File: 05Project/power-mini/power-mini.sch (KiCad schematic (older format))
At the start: 4 parts, among them J1 Conn_01x02, J2 Conn_01x02, U1 GL2576-12TB5T

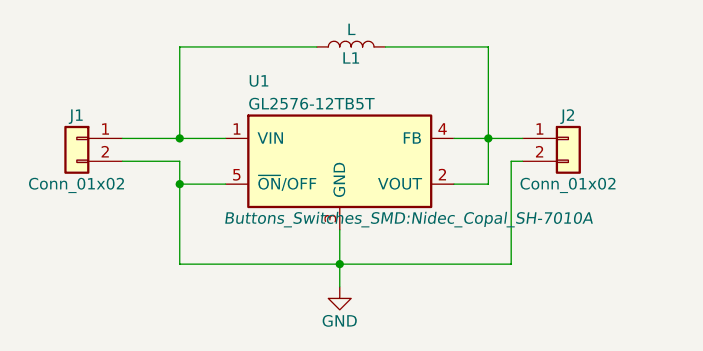
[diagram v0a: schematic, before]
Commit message: Schematic bluetooth Speaker
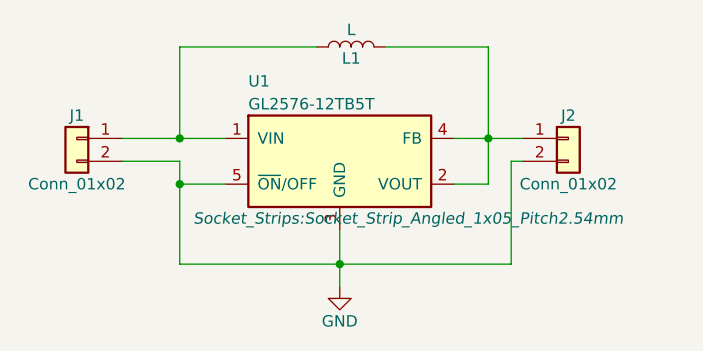
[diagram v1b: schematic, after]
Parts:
- J1: footprint Connectors:Banana_Jack_2Pin -> Connectors:PINHEAD1-2
- J2: footprint Connectors:GS2 -> Connectors:PINHEAD1-2
- L1: footprint Connectors:BNC -> Inductors_THT:L_Axial_L5.3mm_D2.2mm_P2.54mm_Vertical_Vishay_IM-1
- U1: footprint Buttons_Switches_SMD:Nidec_Copal_SH-7010A -> Socket_Strips:Socket_Strip_Angled_1x05_Pitch2.54mm
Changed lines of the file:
@@
 LIBS:valves
 LIBS:dc-dc
+LIBS:open-project
+LIBS:tom_kicad
+LIBS:w_device
+LIBS:esp32-wrover-v3
+LIBS:esp-uno
+LIBS:esp-wroom-32
+LIBS:power-mini-cache
 EELAYER 25 0
 EELAYER END
@@
 F 0 "U1" H 1900 1850 50  0000 L CNN
 F 1 "GL2576-12TB5T" H 1900 1750 50  0000 L CNN
-F 2 "Buttons_Switches_SMD:Nidec_Copal_SH-7010A" H 2600 1250 50  0000 C CIN
+F 2 "Socket_Strips:Socket_Strip_Angled_1x05_Pitch2.54mm" H 2600 1250 50  0000 C CIN
 F 3 "" H 2300 1500 50  0000 C CNN
 	1    2300 1500
@@
 F 0 "J1" H 1150 1500 50  0000 C CNN
 F 1 "Conn_01x02" H 1150 1200 50  0000 C CNN
-F 2 "Connectors:Banana_Jack_2Pin" H 1150 1400 50  0001 C CNN
+F 2 "Connectors:PINHEAD1-2" H 1150 1400 50  0001 C CNN
 F 3 "" H 1150 1400 50  0001 C CNN
 	1    1150 1400
@@
 F 0 "L1" V 2300 1000 50  0000 C CNN
 F 1 "L" V 2425 1000 50  0000 C CNN
-F 2 "Connectors:BNC" H 2350 1000 50  0001 C CNN
+F 2 "Inductors_THT:L_Axial_L5.3mm_D2.2mm_P2.54mm_Vertical_Vishay_IM-1" H 2350 1000 50  0001 C CNN
 F 3 "" H 2350 1000 50  0001 C CNN
 	1    2350 1000
@@
 F 0 "J2" H 3300 1500 50  0000 C CNN
 F 1 "Conn_01x02" H 3300 1200 50  0000 C CNN
-F 2 "Connectors:GS2" H 3300 1400 50  0001 C CNN
+F 2 "Connectors:PINHEAD1-2" H 3300 1400 50  0001 C CNN
 F 3 "" H 3300 1400 50  0001 C CNN
 	1    3300 1400
